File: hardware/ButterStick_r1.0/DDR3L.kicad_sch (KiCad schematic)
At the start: 14 parts, among them U12 MT41K64M16TW-107_J-TR

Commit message: hw.r1d0: Review complete, gerbers generated
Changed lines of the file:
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@@
   (title_block
     (title "ButterStick")
-    (date "2020-07-16")
+    (date "2020-07-17")
     (rev "r1.0")
     (company "GsD")
@@
     (stroke (width 0) (type solid) (color 0 0 0 0))
   )
-  (bus (pts (xy 110.49 66.04) (xy 110.49 68.58))
-    (stroke (width 0) (type solid) (color 0 0 0 0))
-  )
-  (bus (pts (xy 110.49 68.58) (xy 110.49 73.66))
-    (stroke (width 0) (type solid) (color 0 0 0 0))
-  )
-  (bus (pts (xy 110.49 73.66) (xy 110.49 76.2))
-    (stroke (width 0) (type solid) (color 0 0 0 0))
-  )
-  (bus (pts (xy 110.49 76.2) (xy 110.49 81.28))
+  (bus (pts (xy 110.49 66.04) (xy 110.49 71.12))
+    (stroke (width 0) (type solid) (color 0 0 0 0))
+  )
+  (bus (pts (xy 110.49 71.12) (xy 110.49 73.66))
+    (stroke (width 0) (type solid) (color 0 0 0 0))
+  )
+  (bus (pts (xy 110.49 73.66) (xy 110.49 78.74))
+    (stroke (width 0) (type solid) (color 0 0 0 0))
+  )
+  (bus (pts (xy 110.49 78.74) (xy 110.49 81.28))
     (stroke (width 0) (type solid) (color 0 0 0 0))
   )
@@
     (stroke (width 0) (type solid) (color 0 0 0 0))
   )
-  (bus (pts (xy 165.1 90.17) (xy 165.1 92.71))
-    (stroke (width 0) (type solid) (color 0 0 0 0))
-  )
-  (bus (pts (xy 165.1 92.71) (xy 165.1 97.79))
-    (stroke (width 0) (type solid) (color 0 0 0 0))
-  )
-  (bus (pts (xy 165.1 97.79) (xy 165.1 102.87))
-    (stroke (width 0) (type solid) (color 0 0 0 0))
-  )
-  (bus (pts (xy 165.1 102.87) (xy 165.1 105.41))
+  (bus (pts (xy 165.1 90.17) (xy 165.1 95.25))
+    (stroke (width 0) (type solid) (color 0 0 0 0))
+  )
+  (bus (pts (xy 165.1 95.25) (xy 165.1 100.33))
+    (stroke (width 0) (type solid) (color 0 0 0 0))
+  )
+  (bus (pts (xy 165.1 100.33) (xy 165.1 105.41))
     (stroke (width 0) (type solid) (color 0 0 0 0))
   )
@@
     (stroke (width 0) (type solid) (color 0 0 0 0))
   )
-  (bus (pts (xy 165.1 118.11) (xy 165.1 120.65))
-    (stroke (width 0) (type solid) (color 0 0 0 0))
-  )
-  (bus (pts (xy 165.1 120.65) (xy 165.1 125.73))
-    (stroke (width 0) (type solid) (color 0 0 0 0))
-  )
-  (bus (pts (xy 165.1 125.73) (xy 165.1 130.81))
-    (stroke (width 0) (type solid) (color 0 0 0 0))
-  )
-  (bus (pts (xy 165.1 130.81) (xy 165.1 143.51))
-    (stroke (width 0) (type solid) (color 0 0 0 0))
-  )
-  (bus (pts (xy 165.1 143.51) (xy 165.1 149.86))
-    (stroke (width 0) (type solid) (color 0 0 0 0))
-  )
-  (bus (pts (xy 165.1 149.86) (xy 165.1 154.94))
-    (stroke (width 0) (type solid) (color 0 0 0 0))
-  )
+  (bus (pts (xy 165.1 118.11) (xy 165.1 123.19))
+    (stroke (width 0) (type solid) (color 0 0 0 0))
+  )
+  (bus (pts (xy 165.1 123.19) (xy 165.1 128.27))
+    (stroke (width 0) (type solid) (color 0 0 0 0))
+  )
+  (bus (pts (xy 165.1 128.27) (xy 165.1 140.97))
+    (stroke (width 0) (type solid) (color 0 0 0 0))
+  )
+  (bus (pts (xy 165.1 140.97) (xy 165.1 147.32))
+    (stroke (width 0) (type solid) (color 0 0 0 0))
+  )
+  (bus (pts (xy 165.1 147.32) (xy 165.1 154.94))
+    (stroke (width 0) (type solid) (color 0 0 0 0))
+  )

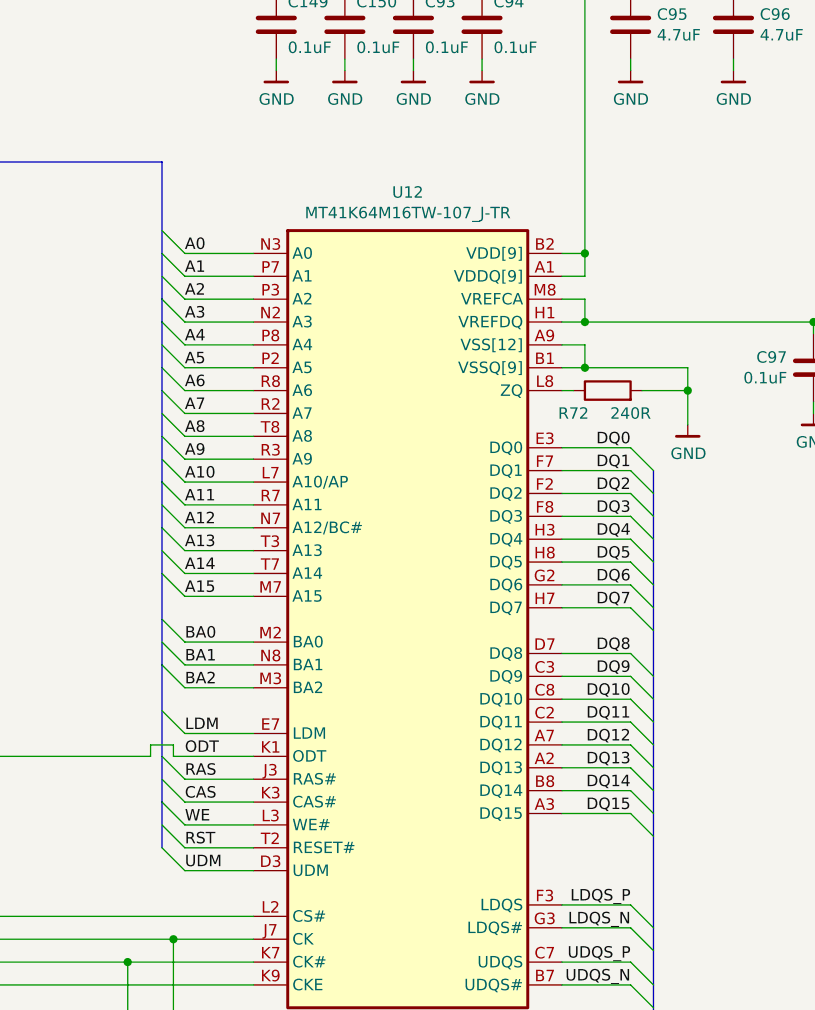
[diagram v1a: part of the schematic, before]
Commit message: hw.r1d0: Update BOM fieids in schematic.
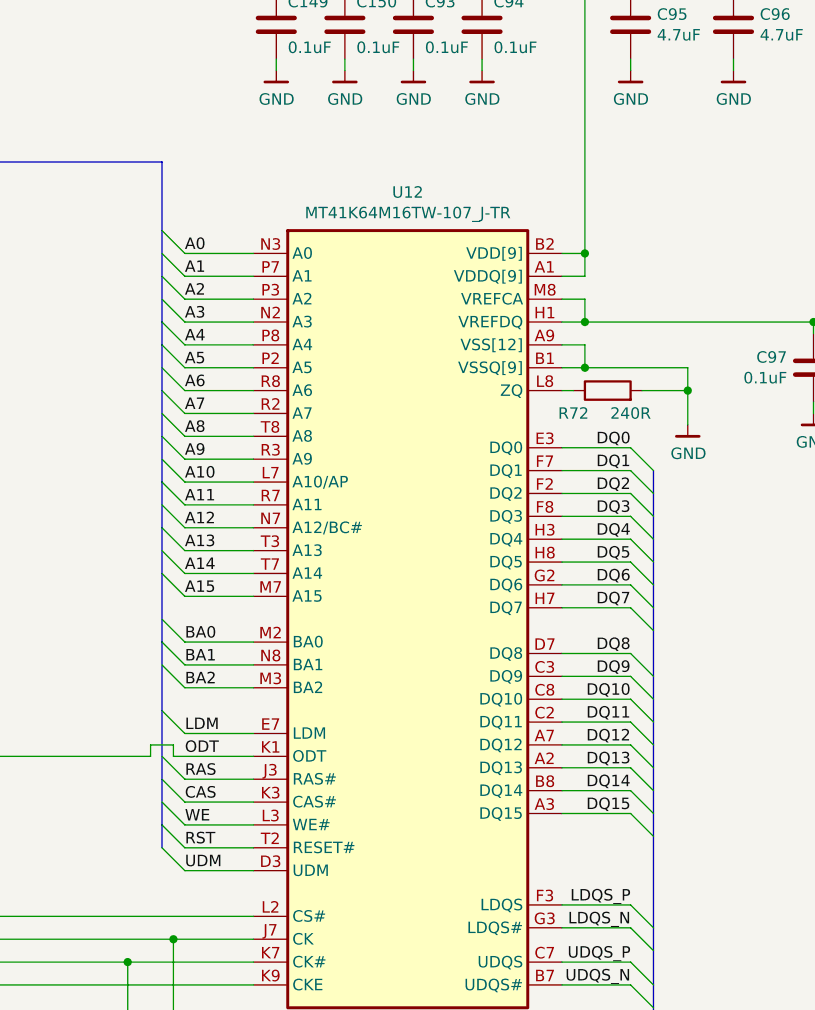
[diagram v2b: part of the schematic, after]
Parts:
- C121, C146, C149, C150, C22, C93, C94, C97: Mfg (none) -> Yageo; PN (none) -> CC0402KRX5R6BB104; Tol (none) -> 10V / X5R
- C95, C96: Mfg (none) -> Yageo; PN (none) -> CC0402MRX5R6BB475
- R71, R94: Mfg (none) -> Yageo; PN (none) -> RC0402FR-0751RL
- R72: Mfg (none) -> Yageo; PN (none) -> RC0402FR-07240RL
- U12: Mfg (none) -> Micron Technology Inc.; PN (none) -> MT41K64M16TW-107:J TR
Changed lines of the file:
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@@
 (kicad_sch (version 20200618) (host eeschema "5.99.0-unknown-73168a9~101~ubuntu18.04.1")
-  (page 14 18)
+  (page 1 18)
   (paper "A4")
   (title_block
@@
     (stroke (width 0) (type solid) (color 0 0 0 0))
   )
-  (bus (pts (xy 110.49 55.88) (xy 110.49 66.04))
-    (stroke (width 0) (type solid) (color 0 0 0 0))
-  )
-  (bus (pts (xy 110.49 66.04) (xy 110.49 71.12))
-    (stroke (width 0) (type solid) (color 0 0 0 0))
-  )
-  (bus (pts (xy 110.49 71.12) (xy 110.49 73.66))
-    (stroke (width 0) (type solid) (color 0 0 0 0))
-  )
-  (bus (pts (xy 110.49 73.66) (xy 110.49 78.74))
-    (stroke (width 0) (type solid) (color 0 0 0 0))
-  )
-  (bus (pts (xy 110.49 78.74) (xy 110.49 81.28))
+  (bus (pts (xy 110.49 55.88) (xy 110.49 63.5))
+    (stroke (width 0) (type solid) (color 0 0 0 0))
+  )
+  (bus (pts (xy 110.49 63.5) (xy 110.49 68.58))
+    (stroke (width 0) (type solid) (color 0 0 0 0))
+  )
+  (bus (pts (xy 110.49 68.58) (xy 110.49 73.66))
+    (stroke (width 0) (type solid) (color 0 0 0 0))
+  )
+  (bus (pts (xy 110.49 73.66) (xy 110.49 76.2))
+    (stroke (width 0) (type solid) (color 0 0 0 0))
+  )
+  (bus (pts (xy 110.49 76.2) (xy 110.49 81.28))
     (stroke (width 0) (type solid) (color 0 0 0 0))
   )
@@
     (stroke (width 0) (type solid) (color 0 0 0 0))
   )
-  (bus (pts (xy 110.49 101.6) (xy 110.49 106.68))
-    (stroke (width 0) (type solid) (color 0 0 0 0))
-  )
-  (bus (pts (xy 110.49 106.68) (xy 110.49 111.76))
-    (stroke (width 0) (type solid) (color 0 0 0 0))
-  )
-  (bus (pts (xy 110.49 111.76) (xy 110.49 121.92))
-    (stroke (width 0) (type solid) (color 0 0 0 0))
-  )
-  (bus (pts (xy 110.49 121.92) (xy 110.49 127))
-    (stroke (width 0) (type solid) (color 0 0 0 0))
-  )
-  (bus (pts (xy 110.49 127) (xy 110.49 132.08))
+  (bus (pts (xy 110.49 101.6) (xy 110.49 109.22))
+    (stroke (width 0) (type solid) (color 0 0 0 0))
+  )
+  (bus (pts (xy 110.49 109.22) (xy 110.49 116.84))
+    (stroke (width 0) (type solid) (color 0 0 0 0))
+  )
+  (bus (pts (xy 110.49 116.84) (xy 110.49 124.46))
+    (stroke (width 0) (type solid) (color 0 0 0 0))
+  )
+  (bus (pts (xy 110.49 124.46) (xy 110.49 129.54))
+    (stroke (width 0) (type solid) (color 0 0 0 0))
+  )
+  (bus (pts (xy 110.49 129.54) (xy 110.49 132.08))
     (stroke (width 0) (type solid) (color 0 0 0 0))
   )
@@
     (stroke (width 0) (type solid) (color 0 0 0 0))
   )
-  (bus (pts (xy 165.1 95.25) (xy 165.1 100.33))
-    (stroke (width 0) (type solid) (color 0 0 0 0))
-  )
-  (bus (pts (xy 165.1 100.33) (xy 165.1 105.41))
+  (bus (pts (xy 165.1 95.25) (xy 165.1 97.79))
+    (stroke (width 0) (type solid) (color 0 0 0 0))
+  )
+  (bus (pts (xy 165.1 97.79) (xy 165.1 102.87))
+    (stroke (width 0) (type solid) (color 0 0 0 0))
+  )
+  (bus (pts (xy 165.1 102.87) (xy 165.1 105.41))
     (stroke (width 0) (type solid) (color 0 0 0 0))
   )
@@
       (effects (font (size 1.27 1.27)) hide)
     )
+    (property "Mfg" "Yageo" (id 4) (at 106.68 162.56 0)
+      (effects (font (size 1.27 1.27)) hide)
+    )
+    (property "PN" "RC0402FR-0751RL" (id 4) (at 106.68 162.56 0)
+      (effects (font (size 1.27 1.27)) hide)
+    )
   )
   (symbol (lib_id "Device:R") (at 111.76 162.56 180)
@@
     )
     (property "Datasheet" "~" (id 3) (at 111.76 162.56 0)
+      (effects (font (size 1.27 1.27)) hide)
+    )
+    (property "Mfg" "Yageo" (id 4) (at 111.76 162.56 0)
+      (effects (font (size 1.27 1.27)) hide)
+    )
+    (property "PN" "RC0402FR-0751RL" (id 4) (at 111.76 162.56 0)
       (effects (font (size 1.27 1.27)) hide)
     )
@@
       (effects (font (size 1.27 1.27)) hide)
     )
+    (property "Mfg" "Yageo" (id 4) (at 160.02 81.28 0)
+      (effects (font (size 1.27 1.27)) hide)
+    )
+    (property "PN" "RC0402FR-07240RL" (id 4) (at 160.02 81.28 0)
+      (effects (font (size 1.27 1.27)) hide)
+    )
   )
   (symbol (lib_id "Device:C") (at 109.22 172.72 0)
@@
       (effects (font (size 1.27 1.27)) hide)
     )
+    (property "Mfg" "Yageo" (id 4) (at 109.22 172.72 0)
+      (effects (font (size 1.27 1.27)) hide)
+    )
+    (property "PN" "CC0402KRX5R6BB104" (id 5) (at 109.22 172.72 0)
+      (effects (font (size 1.27 1.27)) hide)
+    )
+    (property "Tol" "10V / X5R" (id 6) (at 109.22 172.72 0)
+      (effects (font (size 1.27 1.27)) hide)
+    )
   )
   (symbol (lib_id "Device:C") (at 123.19 40.64 0)
@@
       (effects (font (size 1.27 1.27)) hide)
     )
+    (property "Mfg" "Yageo" (id 4) (at 123.19 40.64 0)
+      (effects (font (size 1.27 1.27)) hide)
+    )
+    (property "PN" "CC0402KRX5R6BB104" (id 5) (at 123.19 40.64 0)
+      (effects (font (size 1.27 1.27)) hide)
+    )
+    (property "Tol" "10V / X5R" (id 6) (at 123.19 40.64 0)
+      (effects (font (size 1.27 1.27)) hide)
+    )
   )
   (symbol (lib_id "Device:C") (at 130.81 40.64 0)
@@
       (effects (font (size 1.27 1.27)) hide)
     )
+    (property "Mfg" "Yageo" (id 4) (at 130.81 40.64 0)
+      (effects (font (size 1.27 1.27)) hide)
+    )
+    (property "PN" "CC0402KRX5R6BB104" (id 5) (at 130.81 40.64 0)
+      (effects (font (size 1.27 1.27)) hide)
+    )
+    (property "Tol" "10V / X5R" (id 6) (at 130.81 40.64 0)
+      (effects (font (size 1.27 1.27)) hide)
+    )
   )
   (symbol (lib_id "Device:C") (at 138.43 40.64 0)
@@
       (effects (font (size 1.27 1.27)) hide)
     )
+    (property "Mfg" "Yageo" (id 4) (at 138.43 40.64 0)
+      (effects (font (size 1.27 1.27)) hide)
+    )
+    (property "PN" "CC0402KRX5R6BB104" (id 5) (at 138.43 40.64 0)
+      (effects (font (size 1.27 1.27)) hide)
+    )
+    (property "Tol" "10V / X5R" (id 6) (at 138.43 40.64 0)
+      (effects (font (size 1.27 1.27)) hide)
+    )
   )
   (symbol (lib_id "Device:C") (at 146.05 40.64 0)
@@
       (effects (font (size 1.27 1.27)) hide)
     )
+    (property "Mfg" "Yageo" (id 4) (at 146.05 40.64 0)
+      (effects (font (size 1.27 1.27)) hide)
+    )
+    (property "PN" "CC0402KRX5R6BB104" (id 5) (at 146.05 40.64 0)
+      (effects (font (size 1.27 1.27)) hide)
+    )
+    (property "Tol" "10V / X5R" (id 6) (at 146.05 40.64 0)
+      (effects (font (size 1.27 1.27)) hide)
+    )
   )
   (symbol (lib_id "Device:C") (at 162.56 40.64 0)
@@
       (effects (font (size 1.27 1.27)) hide)
     )
+    (property "Mfg" "Yageo" (id 4) (at 162.56 40.64 0)
+      (effects (font (size 1.27 1.27)) hide)
+    )
+    (property "PN" "CC0402MRX5R6BB475" (id 4) (at 162.56 40.64 0)
+      (effects (font (size 1.27 1.27)) hide)
+    )
   )
   (symbol (lib_id "Device:C") (at 173.99 40.64 0)
@@
     )
     (property "Datasheet" "~" (id 3) (at 173.99 40.64 0)
+      (effects (font (size 1.27 1.27)) hide)
+    )
+    (property "Mfg" "Yageo" (id 4) (at 173.99 40.64 0)
+      (effects (font (size 1.27 1.27)) hide)
+    )
+    (property "PN" "CC0402MRX5R6BB475" (id 4) (at 173.99 40.64 0)
       (effects (font (size 1.27 1.27)) hide)
     )
@@
       (effects (font (size 1.27 1.27)) hide)
     )
+    (property "Mfg" "Yageo" (id 4) (at 182.88 78.74 0)
+      (effects (font (size 1.27 1.27)) hide)
+    )
+    (property "PN" "CC0402KRX5R6BB104" (id 5) (at 182.88 78.74 0)
+      (effects (font (size 1.27 1.27)) hide)
+    )
+    (property "Tol" "10V / X5R" (id 6) (at 182.88 78.74 0)
+      (effects (font (size 1.27 1.27)) hide)
+    )
   )
   (symbol (lib_id "Device:C") (at 189.23 78.74 0)
@@
       (effects (font (size 1.27 1.27)) hide)
     )
+    (property "Mfg" "Yageo" (id 4) (at 189.23 78.74 0)
+      (effects (font (size 1.27 1.27)) hide)
+    )
+    (property "PN" "CC0402KRX5R6BB104" (id 5) (at 189.23 78.74 0)
+      (effects (font (size 1.27 1.27)) hide)
+    )
+    (property "Tol" "10V / X5R" (id 6) (at 189.23 78.74 0)
+      (effects (font (size 1.27 1.27)) hide)
+    )
   )
   (symbol (lib_id "Device:C") (at 201.93 78.74 0)
@@
     )
     (property "Datasheet" "~" (id 3) (at 201.93 78.74 0)
+      (effects (font (size 1.27 1.27)) hide)
+    )
+    (property "Mfg" "Yageo" (id 4) (at 201.93 78.74 0)
+      (effects (font (size 1.27 1.27)) hide)
+    )
+    (property "PN" "CC0402KRX5R6BB104" (id 5) (at 201.93 78.74 0)
+      (effects (font (size 1.27 1.27)) hide)
+    )
+    (property "Tol" "10V / X5R" (id 6) (at 201.93 78.74 0)
       (effects (font (size 1.27 1.27)) hide)
     )
@@
       (effects (font (size 1.27 1.27)) hide)
     )
+    (property "Mfg" "Micron Technology Inc." (id 4) (at 137.16 96.52 0)
+      (effects (font (size 1.27 1.27)) hide)
+    )
+    (property "PN" "MT41K64M16TW-107:J TR" (id 5) (at 137.16 96.52 0)
+      (effects (font (size 1.27 1.27)) hide)
+    )
